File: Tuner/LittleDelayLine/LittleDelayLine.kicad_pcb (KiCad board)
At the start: 2 copper layers, 100 x 100 mm, 117 parts, among them J1 Conn_Coaxial, J10 Conn_Coaxial, J11 Conn_02x05_Odd_Even, J12 Conn_01x01, J13 Conn_01x01, J14 Conn_01x01, J15 Conn_01x01, J16 Conn_01x01, J17 Conn_Coaxial, J18 Conn_01x01, J19 Conn_01x01, J2 Conn_Coaxial, J20 Conn_01x01, J21 Conn_01x01, J22 Conn_Coaxial, J23 Conn_Coaxial, J24 Conn_Coaxial, J25 Conn_01x01, J26 Conn_01x01, J27 Conn_01x01, J28 Conn_01x01, J3 Conn_Coaxial, J4 Conn_Coaxial, J5 Conn_Coaxial, J6 Conn_Coaxial, J7 Conn_Coaxial, J8 Conn_Coaxial, J9 Conn_Coaxial, P10 Conn_01x01, P11 Conn_01x01, P12 Conn_01x01, P2 Conn_01x01, P3 Conn_01x01, P4 Conn_01x01, P5 Conn_01x01, P6 Conn_01x01, P7 Conn_01x01, P8 Conn_01x01, P9 Conn_01x01, U1 MCP23008, U2 ULN2803A

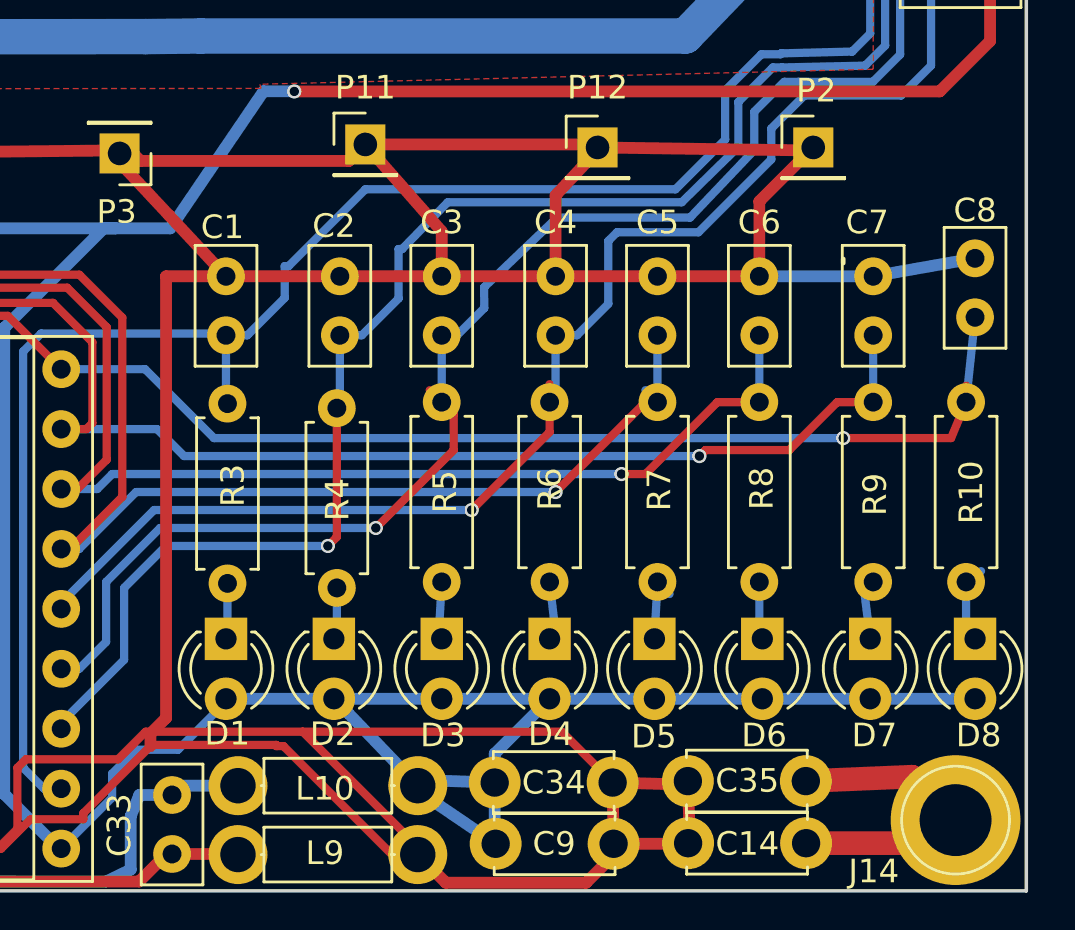
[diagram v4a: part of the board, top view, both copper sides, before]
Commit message: Added yet more ground connections
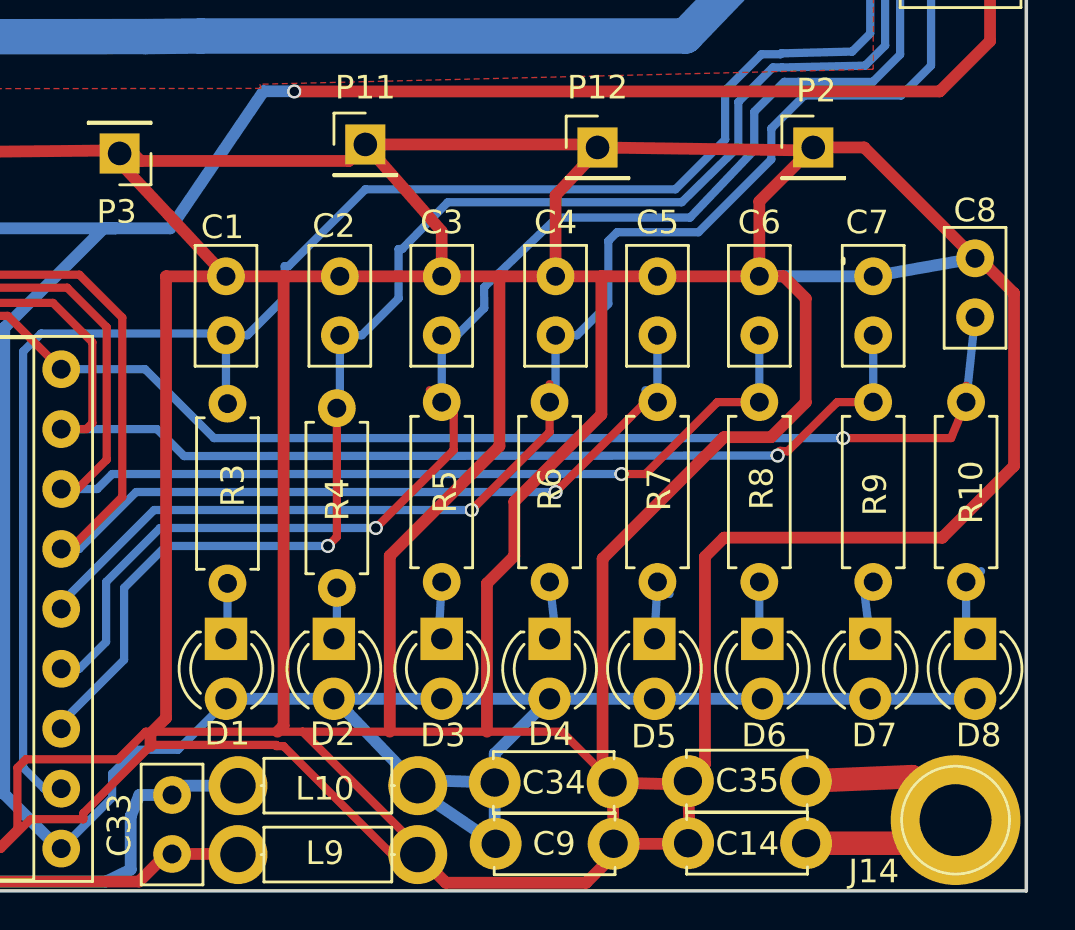
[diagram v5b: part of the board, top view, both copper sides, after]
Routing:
- net RLYGND: track 265.6 -> 398.2 mm
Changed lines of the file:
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@@
     (thickness 1.6)
     (drawings 41)
-    (tracks 900)
+    (tracks 934)
     (zones 0)
     (modules 117)
@@
   )
   (setup
-    (last_trace_width 0.25)
+    (last_trace_width 0.5)
     (user_trace_width 0.35)
     (user_trace_width 0.5)
@@
   (segment (start 109.093 130.429) (end 113.157 130.429) (width 0.35) (layer B.Cu) (net 17) (status 10))
   (segment (start 141.986 129.286) (end 143.51 129.286) (width 0.35) (layer F.Cu) (net 17) (status 20))
-  (segment (start 139.954 131.318) (end 141.986 129.286) (width 0.35) (layer F.Cu) (net 17))
-  (segment (start 136.398 131.318) (end 139.954 131.318) (width 0.35) (layer F.Cu) (net 17))
-  (segment (start 136.144 131.572) (end 136.398 131.318) (width 0.35) (layer F.Cu) (net 17))
-  (via (at 136.144 131.572) (size 0.6) (drill 0.4) (layers F.Cu B.Cu) (net 17))
-  (segment (start 114.3 131.572) (end 136.144 131.572) (width 0.35) (layer B.Cu) (net 17))
+  (segment (start 139.88 131.37) (end 141.986 129.286) (width 0.35) (layer F.Cu) (net 17))
+  (segment (start 139.56 131.35) (end 139.88 131.37) (width 0.35) (layer F.Cu) (net 17))
+  (segment (start 139.46 131.55) (end 139.56 131.35) (width 0.35) (layer F.Cu) (net 17))
+  (via (at 139.46 131.55) (size 0.6) (drill 0.4) (layers F.Cu B.Cu) (net 17))
+  (segment (start 114.3 131.572) (end 139.46 131.55) (width 0.35) (layer B.Cu) (net 17))
   (segment (start 113.157 130.429) (end 114.3 131.572) (width 0.35) (layer B.Cu) (net 17))
   (segment (start 143.51 126.452) (end 143.51 129.286) (width 0.35) (layer B.Cu) (net 17) (status 30))
@@
   (segment (start 148.463 138.684) (end 147.828 139.319) (width 0.35) (layer B.Cu) (net 30) (status 30))
   (segment (start 147.9296 136.6012) (end 148.082 136.4488) (width 0.35) (layer B.Cu) (net 30) (status 30))
+  (segment (start 118.52 123.952) (end 118.52 143) (width 0.5) (layer F.Cu) (net 31))
+  (segment (start 118.52 143) (end 118.264 143.256) (width 0.5) (layer F.Cu) (net 31))
+  (segment (start 131.99 123.952) (end 131.99 129.81) (width 0.5) (layer F.Cu) (net 31))
+  (segment (start 127.14 136.97) (end 127.14 143.256) (width 0.5) (layer F.Cu) (net 31))
+  (segment (start 128.3 135.81) (end 127.14 136.97) (width 0.5) (layer F.Cu) (net 31))
+  (segment (start 128.3 133.5) (end 128.3 135.81) (width 0.5) (layer F.Cu) (net 31))
+  (segment (start 131.99 129.81) (end 128.3 133.5) (width 0.5) (layer F.Cu) (net 31))
+  (segment (start 127.67 123.952) (end 127.67 131.15) (width 0.5) (layer F.Cu) (net 31))
+  (segment (start 123.02 135.8) (end 123.02 143.256) (width 0.5) (layer F.Cu) (net 31))
+  (segment (start 127.67 131.15) (end 123.02 135.8) (width 0.5) (layer F.Cu) (net 31))
+  (segment (start 138.684 123.952) (end 139.712 123.952) (width 0.5) (layer F.Cu) (net 31))
+  (segment (start 132.04 135.92) (end 132.04 144.98256) (width 0.5) (layer F.Cu) (net 31))
+  (segment (start 137.19 130.77) (end 132.04 135.92) (width 0.5) (layer F.Cu) (net 31))
+  (segment (start 139.18 130.77) (end 137.19 130.77) (width 0.5) (layer F.Cu) (net 31))
+  (segment (start 140.65 129.3) (end 139.18 130.77) (width 0.5) (layer F.Cu) (net 31))
+  (segment (start 140.65 124.89) (end 140.65 129.3) (width 0.5) (layer F.Cu) (net 31))
+  (segment (start 139.712 123.952) (end 140.65 124.89) (width 0.5) (layer F.Cu) (net 31))
+  (segment (start 132.04 144.98256) (end 132.46736 145.40992) (width 0.5) (layer F.Cu) (net 31))
+  (segment (start 147.828 123.19) (end 148 123.19) (width 0.5) (layer F.Cu) (net 31))
+  (segment (start 148 123.19) (end 149.48 124.67) (width 0.5) (layer F.Cu) (net 31))
+  (segment (start 136.38 135.84) (end 136.38 144.624) (width 0.5) (layer F.Cu) (net 31))
+  (segment (start 137.19 135.03) (end 136.38 135.84) (width 0.5) (layer F.Cu) (net 31))
+  (segment (start 146.44 135.03) (end 137.19 135.03) (width 0.5) (layer F.Cu) (net 31))
+  (segment (start 149.48 131.99) (end 146.44 135.03) (width 0.5) (layer F.Cu) (net 31))
+  (segment (start 149.48 124.67) (end 149.48 131.99) (width 0.5) (layer F.Cu) (net 31))
+  (segment (start 136.38 144.624) (end 135.65504 145.34896) (width 0.5) (layer F.Cu) (net 31))
+  (segment (start 140.97 118.491) (end 143.129 118.491) (width 0.5) (layer F.Cu) (net 31))
+  (segment (start 143.129 118.491) (end 147.828 123.19) (width 0.5) (layer F.Cu) (net 31))
   (segment (start 105.029 118.6815) (end 98.298 118.6815) (width 0.5) (layer F.Cu) (net 31) (status 30))
   (segment (start 98.298 118.6815) (end 98.1075 118.491) (width 0.5) (layer F.Cu) (net 31) (status 30))
@@
   (segment (start 98.1075 118.491) (end 90.9955 118.491) (width 0.5) (layer F.Cu) (net 31) (status 30))
   (segment (start 90.9955 118.491) (end 90.805 118.3005) (width 0.5) (layer F.Cu) (net 31) (status 30))
-  (segment (start 119.3292 143.256) (end 130.31344 143.256) (width 0.35) (layer F.Cu) (net 31))
+  (segment (start 119.3292 143.256) (end 123.02 143.256) (width 0.35) (layer F.Cu) (net 31))
+  (segment (start 123.02 143.256) (end 127.14 143.256) (width 0.35) (layer F.Cu) (net 31))
+  (segment (start 127.14 143.256) (end 130.31344 143.256) (width 0.35) (layer F.Cu) (net 31))
   (segment (start 130.31344 143.256) (end 132.46736 145.40992) (width 0.35) (layer F.Cu) (net 31) (status 20))
   (segment (start 118.2116 143.8656) (end 118.5164 143.8656) (width 0.35) (layer F.Cu) (net 31))
@@
   (segment (start 118.2116 143.8148) (end 118.2116 143.8656) (width 0.35) (layer F.Cu) (net 31))
   (segment (start 101.473 148.209) (end 106.4006 148.209) (width 0.35) (layer F.Cu) (net 31) (status 10))
-  (segment (start 119.3292 143.256) (end 124.206 148.1328) (width 0.35) (layer F.Cu) (net 31) (status 20))
-  (segment (start 112.6744 143.256) (end 119.3292 143.256) (width 0.35) (layer F.Cu) (net 31))
-  (segment (start 111.506 144.4244) (end 112.6744 143.256) (width 0.35) (layer F.Cu) (net 31))
-  (segment (start 107.5944 144.4244) (end 111.506 144.4244) (width 0.35) (layer F.Cu) (net 31))
-  (segment (start 107.2388 144.78) (end 107.5944 144.4244) (width 0.35) (layer F.Cu) (net 31))
-  (segment (start 107.2388 147.3708) (end 107.2388 144.78) (width 0.35) (layer F.Cu) (net 31))
   (segment (start 106.4006 148.209) (end 107.2388 147.3708) (width 0.35) (layer F.Cu) (net 31))
+  (segment (start 107.2388 147.3708) (end 107.2388 144.78) (width 0.35) (layer F.Cu) (net 31))
+  (segment (start 107.2388 144.78) (end 107.5944 144.4244) (width 0.35) (layer F.Cu) (net 31))
+  (segment (start 107.5944 144.4244) (end 111.506 144.4244) (width 0.35) (layer F.Cu) (net 31))
+  (segment (start 111.506 144.4244) (end 112.6744 143.256) (width 0.35) (layer F.Cu) (net 31))
+  (segment (start 112.6744 143.256) (end 118.264 143.256) (width 0.35) (layer F.Cu) (net 31))
+  (segment (start 119.3292 143.256) (end 124.206 148.1328) (width 0.35) (layer F.Cu) (net 31) (status 20))
+  (segment (start 118.264 143.256) (end 119.3292 143.256) (width 0.35) (layer F.Cu) (net 31))
   (segment (start 124.206 148.1328) (end 124.206 148.463) (width 0.35) (layer F.Cu) (net 31) (status 30))
   (segment (start 135.65504 145.34896) (end 135.7414 147.9042) (width 0.5) (layer F.Cu) (net 31) (status 30))
@@
   (segment (start 143.51 123.952) (end 138.684 123.952) (width 0.5) (layer B.Cu) (net 31) (status 30))
   (segment (start 134.366 123.952) (end 138.684 123.952) (width 0.5) (layer F.Cu) (net 31) (status 30))
-  (segment (start 130.048 123.952) (end 134.366 123.952) (width 0.5) (layer F.Cu) (net 31) (status 30))
-  (segment (start 125.222 123.952) (end 130.048 123.952) (width 0.5) (layer F.Cu) (net 31) (status 30))
+  (segment (start 130.048 123.952) (end 131.99 123.952) (width 0.5) (layer F.Cu) (net 31) (status 30))
+  (segment (start 131.99 123.952) (end 134.366 123.952) (width 0.5) (layer F.Cu) (net 31) (status 30))
+  (segment (start 125.222 123.952) (end 127.67 123.952) (width 0.5) (layer F.Cu) (net 31) (status 30))
+  (segment (start 127.67 123.952) (end 130.048 123.952) (width 0.5) (layer F.Cu) (net 31) (status 30))
   (segment (start 120.904 123.952) (end 125.222 123.952) (width 0.5) (layer F.Cu) (net 31) (status 30))
-  (segment (start 116.078 123.952) (end 120.904 123.952) (width 0.5) (layer F.Cu) (net 31) (status 30))
+  (segment (start 116.078 123.952) (end 118.52 123.952) (width 0.5) (layer F.Cu) (net 31) (status 30))
+  (segment (start 118.52 123.952) (end 120.904 123.952) (width 0.5) (layer F.Cu) (net 31) (status 30))
   (segment (start 116.078 123.952) (end 113.538 123.952) (width 0.5) (layer F.Cu) (net 31) (status 10))
   (segment (start 101.6 148.082) (end 101.473 148.209) (width 0.5) (layer F.Cu) (net 31) (status 30))
